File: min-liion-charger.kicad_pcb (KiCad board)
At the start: 2 copper layers, 18.5 x 15.1 mm, 11 parts, among them J1 Conn_01x02, J2 Conn_01x03, U1 bq21040

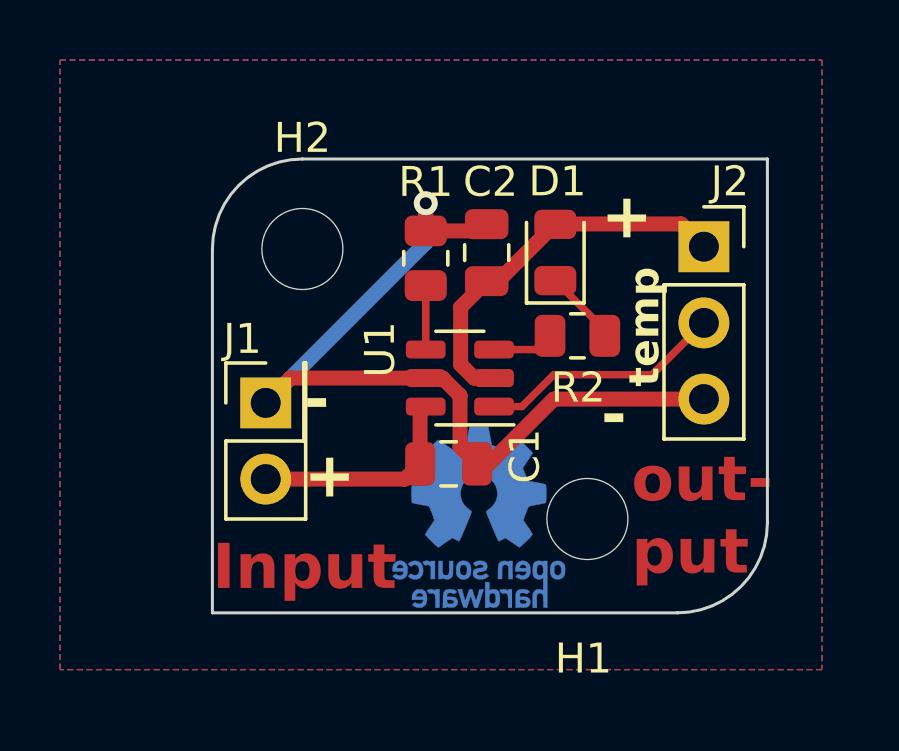
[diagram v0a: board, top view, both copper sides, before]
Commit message: shrink, better silkscreen
Signed-off-by: Marcus Müller <marcus@hostalia.de>
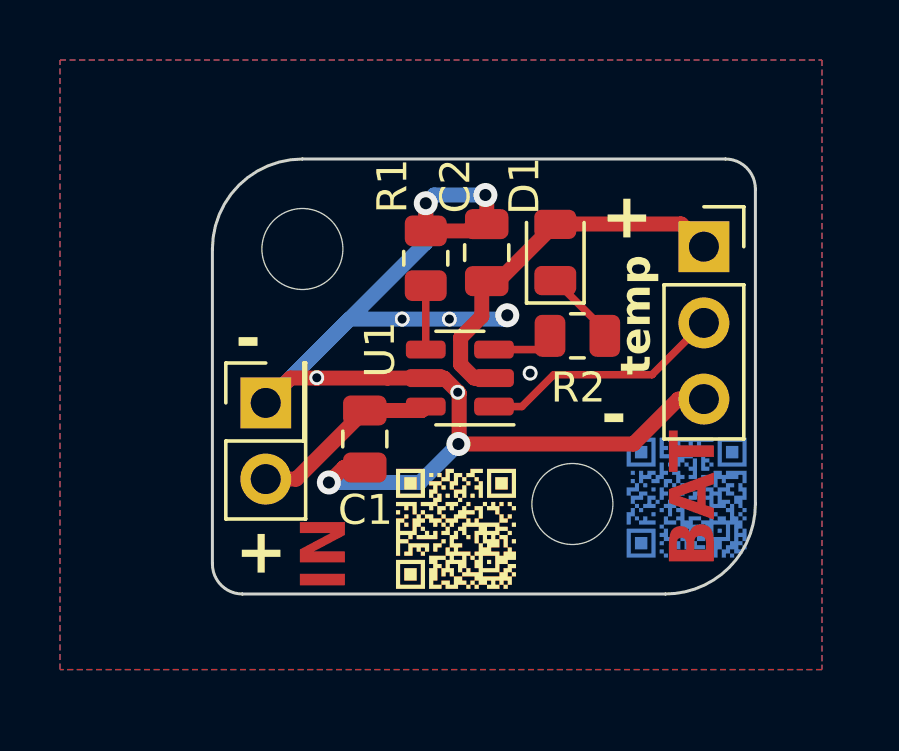
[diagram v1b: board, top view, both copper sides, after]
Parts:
- removed SYM2: Logo_Open_Hardware_Small, Symbol:OSHW-Logo_5.7x6mm_Copper
- added oshwlogo1: Logo_Open_Hardware_Small, Symbol:OSHW-Logo_5.7x6mm_SilkScreen, B.Cu at (132.8, 91.1)
- added qrcode-copper-bottom1: SYM_Arrow_Small, QR:qr-copper, B.Cu at (140.8, 88.8)
- added qrcode-copper-top1: SYM_Arrow_Small, QR:qr-copper, F.Cu at (133.1, 89.8)
- added qrcode1: SYM_Arrow_Small, QR:QR code, F.Cu at (133.1, 89.8)
- moved C1 2.91 mm to (132.1, 88.8), turned to -90 degrees
- moved H1 0.71 mm to (139.0, 91.0)
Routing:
- net GND: track 30.3 -> 47.2 mm, vias 1 -> 10
- net VCC: track 7.34 -> 6.34 mm
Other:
- board size 18.5 x 15.1 mm -> 18.1 x 14.5 mm
- board text added: "(c) 2023 Marcus Müller licensed under CERN OHL-S 2.0"
- board text added: "BAT"
- board text added: "IN"
- board text added: "https://github.com/ marcusmueller/ min-liion-charger"
- board text removed: "(c) 2023 Marcus Müller under CERN OHLv2"
- board text removed: "Input"
- board text removed: "out- put"

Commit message: slightly increase Y-size to slip into cheaper panelize-by-jlcpcb regime
Signed-off-by: Marcus Müller <marcus@hostalia.de>
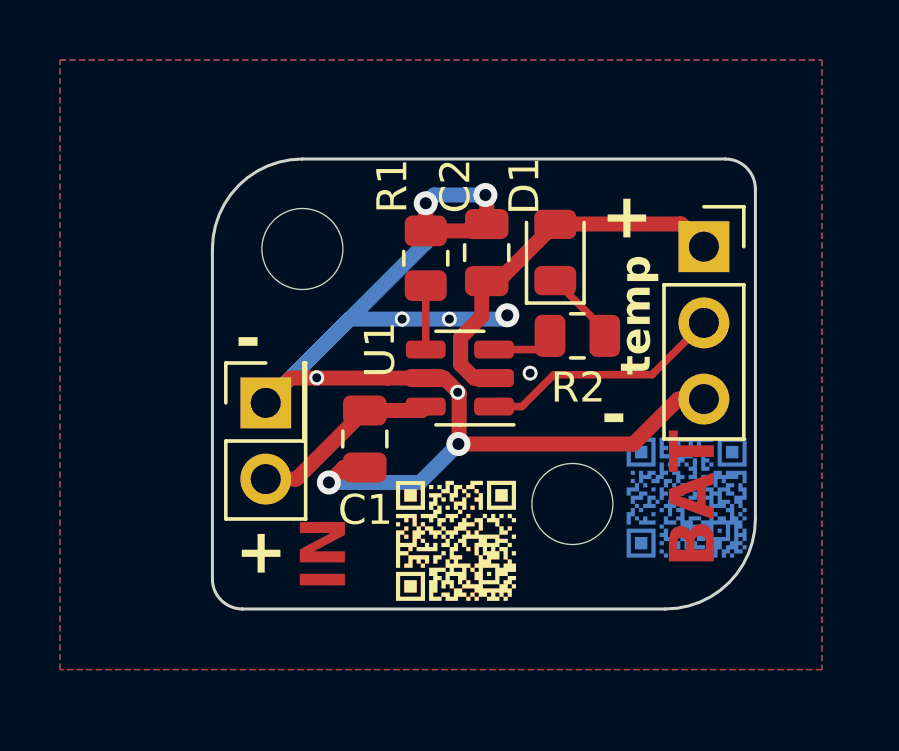
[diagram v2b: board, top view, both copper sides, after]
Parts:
- moved qrcode-copper-top1 0.40 mm to (133.1, 90.2)
- moved qrcode1 0.40 mm to (133.1, 90.2)
- moved oshwlogo1 0.30 mm to (132.8, 91.4)
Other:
- board size 18.1 x 14.5 mm -> 18.1 x 15 mm
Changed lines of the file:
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@@
   )
   (footprint "QR:QR code" (layer "F.Cu")
-    (at 133.13046 89.821624)
+    (at 133.13046 90.221624)
     (property "Sheetfile" "min-liion-charger.kicad_sch")
     (property "Sheetname" "")
@@
   )
   (footprint "QR:qr-copper" (layer "F.Cu")
-    (at 133.13046 89.821624)
+    (at 133.13046 90.221624)
     (property "Sheetfile" "min-liion-charger.kicad_sch")
     (property "Sheetname" "")
@@
   )
   (footprint "Symbol:OSHW-Logo_5.7x6mm_SilkScreen" (layer "B.Cu")
-    (at 132.8 91.1 90)
+    (at 132.8 91.4 90)
     (descr "Open Source Hardware Logo")
     (tags "Logo OSHW")
@@
       (stroke (width 0.01) (type solid)) (fill solid) (layer "B.SilkS"))
   )
-  (gr_line (start 127 93) (end 127 82.5)
+  (gr_line (start 127 93.5) (end 127 82.5)
     (stroke (width 0.1) (type default)) (layer "Edge.Cuts"))
-  (gr_arc (start 145.1 91) (mid 144.221327 93.121333) (end 142.1 94)
+  (gr_arc (start 145.1 91.5) (mid 144.22132 93.62132) (end 142.1 94.5)
     (stroke (width 0.1) (type default)) (layer "Edge.Cuts"))
-  (gr_line (start 142.1 94) (end 128 94)
+  (gr_line (start 142.1 94.5) (end 128 94.5)
     (stroke (width 0.1) (type default)) (layer "Edge.Cuts"))
   (gr_line (start 130 79.5) (end 144.1 79.5)
@@
   (gr_arc (start 127 82.5) (mid 127.87868 80.37868) (end 130 79.5)
     (stroke (width 0.1) (type default)) (layer "Edge.Cuts"))
-  (gr_arc (start 128 94) (mid 127.292894 93.707107) (end 127 93)
+  (gr_arc (start 128 94.5) (mid 127.292893 94.207107) (end 127 93.5)
     (stroke (width 0.1) (type default)) (layer "Edge.Cuts"))
   (gr_arc (start 144.1 79.5) (mid 144.807106 79.792893) (end 145.1 80.5)
     (stroke (width 0.1) (type default)) (layer "Edge.Cuts"))
-  (gr_line (start 145.1 80.5) (end 145.1 91)
+  (gr_line (start 145.1 80.5) (end 145.1 91.5)
     (stroke (width 0.1) (type default)) (layer "Edge.Cuts"))
   (gr_text "BAT" (at 143.9 93.1 90) (layer "F.Cu")
